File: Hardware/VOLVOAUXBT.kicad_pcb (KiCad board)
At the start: 2 copper layers, 100 x 35 mm, 66 parts, among them J1 10118193-0001LF, J10 Conn_01x02_Pin, J11 Conn_01x02_Pin, J12 Conn_01x05_Pin, J13 Conn_01x05_Pin, J14 Conn_01x05_Pin, J15 Conn_01x02_Pin, J16 Conn_01x02_Pin, J17 Conn_01x01_Pin, J18 Conn_01x02_Pin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

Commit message: Before swap to wroom
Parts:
- moved C2 122.7 mm to (161.3, 139.5), turned to -90 degrees
- moved C1 117.8 mm to (158.8, 139.5), turned to -90 degrees
- moved U1 109.0 mm to (156.2, 137.2), turned to 180 degrees
- moved C4 105.6 mm to (153.3, 141.0), turned to 0 degrees
- moved C3 104.1 mm to (153.3, 138.5), turned to 0 degrees
- moved J11 86.3 mm to (160.0, 144.8), turned to -90 degrees
- moved C10 79.2 mm to (147.3, 101.6), turned to 0 degrees
- moved C11 78.8 mm to (147.3, 99.1), turned to 0 degrees
- moved C20 77.6 mm to (141.8, 143.5), turned to 180 degrees
- moved C21 77.3 mm to (139.3, 145.6), turned to -90 degrees
- moved R10 76.9 mm to (146.1, 91.9), turned to -90 degrees
- moved C14 75.5 mm to (145.7, 96.5), turned to 0 degrees
- moved C17 74.3 mm to (143.5, 86.4), turned to 0 degrees
- moved R12 72.3 mm to (139.3, 142.2), turned to -90 degrees
- moved J18 71.9 mm to (138.0, 148.6), turned to -90 degrees
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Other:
- board size 100 x 35 mm -> 110 x 30 mm

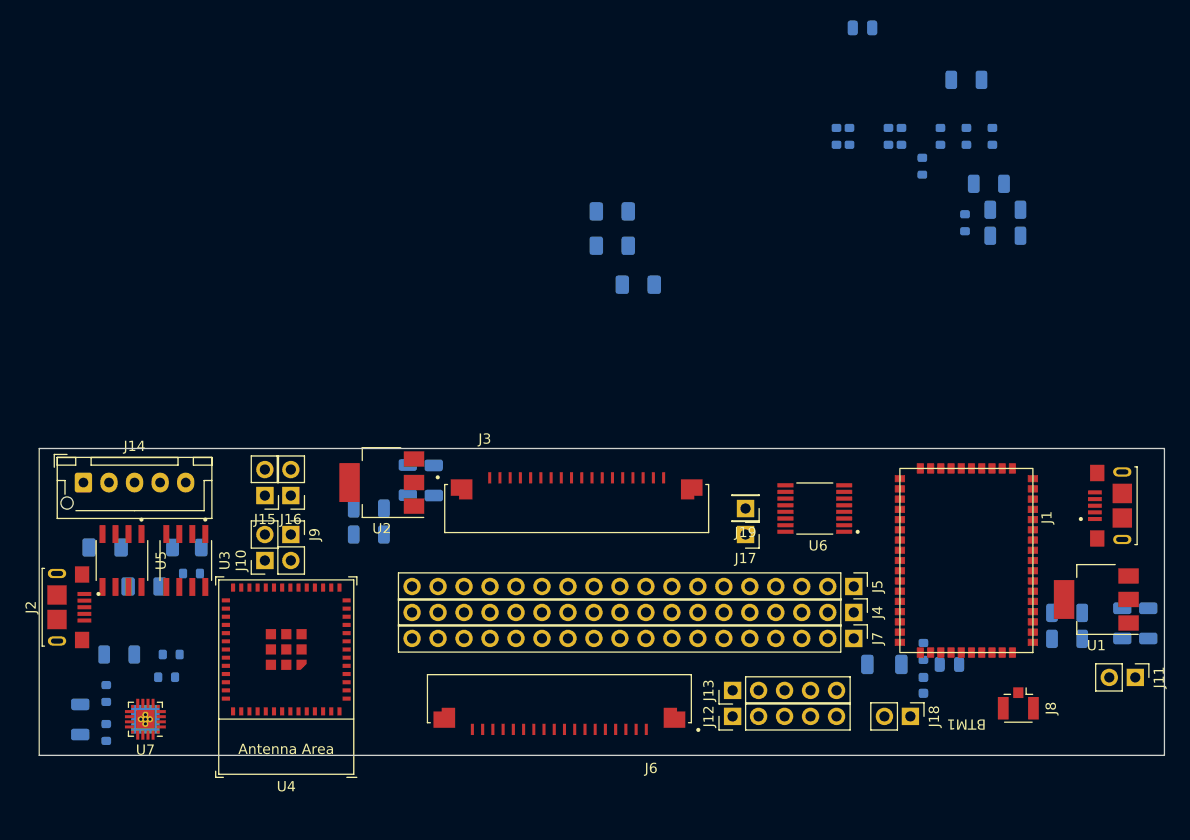
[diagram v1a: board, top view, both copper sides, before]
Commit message: Swap to ESP32-wroom-32e. Updated PCB too
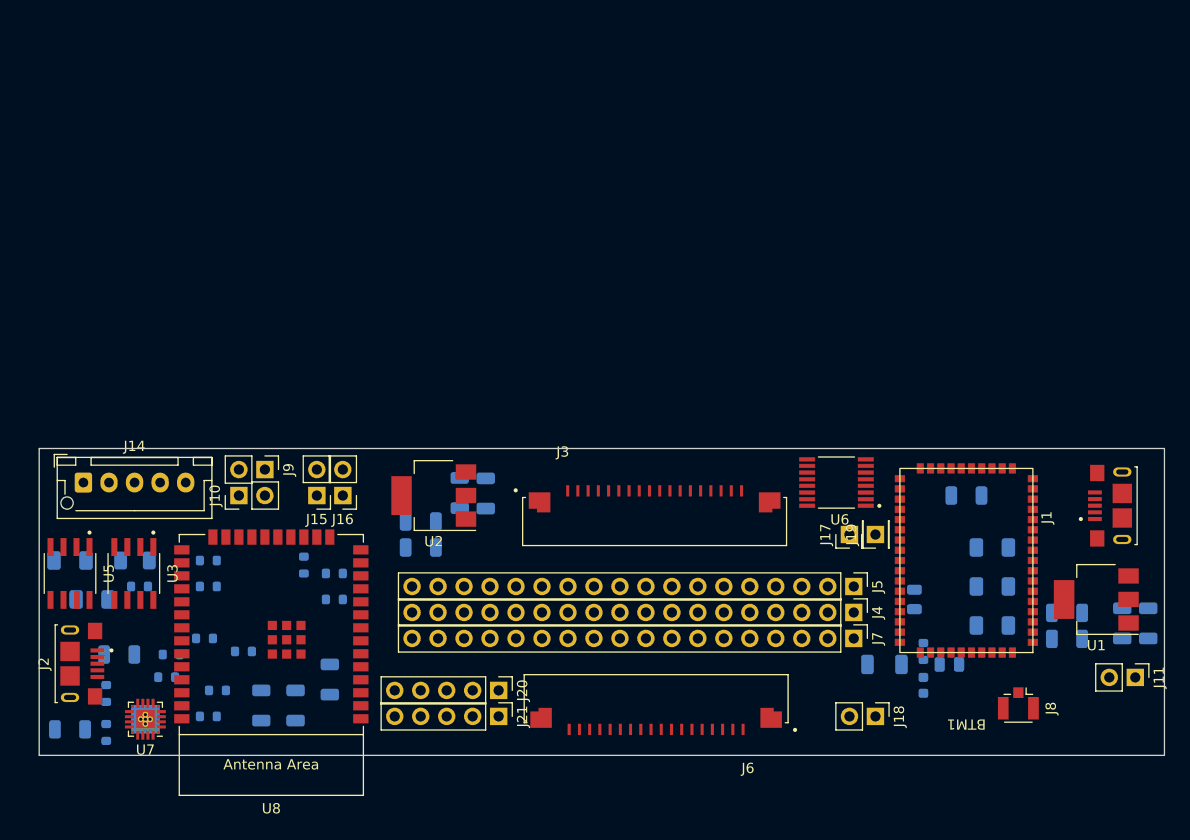
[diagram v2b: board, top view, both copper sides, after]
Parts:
- removed C10: 10uF/25V(20%), Capacitor_SMD:C_1206_3216Metric
- removed C11: 0.1uF/50V(10%), Capacitor_SMD:C_1206_3216Metric
- removed C14: 1uF/16V(10%), Capacitor_SMD:C_1206_3216Metric
- removed J12, J13: Conn_01x05_Pin, Connector_PinHeader_2.54mm:PinHeader_1x05_P2.54mm_Vertical
- removed R1: 10K(1%), Resistor_SMD:R_0603_1608Metric
- removed R10, R3, R4, R5, R6, R7, R8, R9: 500, Resistor_SMD:R_0603_1608Metric
- removed U4: ESP32-MINI-1, PCM_Espressif:ESP32-MINI-1
- added C23: 1uF/16V(10%), Capacitor_SMD:C_1206_3216Metric, B.Cu at (81.3, 145.0)
- added C24: 10uF/25V(20%), Capacitor_SMD:C_1206_3216Metric, B.Cu at (77.9, 147.5)
- added C25: 0.1uF/50V(10%), Capacitor_SMD:C_1206_3216Metric, B.Cu at (74.6, 147.5)
- added J20: Conn_01x05_Pin, Connector_PinHeader_2.54mm:PinHeader_1x05_P2.54mm_Vertical, F.Cu at (97.8, 146.1)
- added J21: Conn_01x05_Pin, Connector_PinHeader_2.54mm:PinHeader_1x05_P2.54mm_Vertical, F.Cu at (97.8, 148.6)
- added R16: 10K(1%), Resistor_SMD:R_0603_1608Metric, B.Cu at (72.8, 142.2)
- added R17: 500, Resistor_SMD:R_0603_1608Metric, B.Cu at (78.7, 133.8)
- added R18: 500, Resistor_SMD:R_0603_1608Metric, B.Cu at (81.7, 134.6)
- added R19: 500, Resistor_SMD:R_0603_1608Metric, B.Cu at (69.4, 148.6)
- added R20: 500, Resistor_SMD:R_0603_1608Metric, B.Cu at (81.7, 137.2)
- added R21: 500, Resistor_SMD:R_0603_1608Metric, B.Cu at (69.4, 133.3)
- added R22: 500, Resistor_SMD:R_0603_1608Metric, B.Cu at (69.4, 135.9)
- added R23: 500, Resistor_SMD:R_0603_1608Metric, B.Cu at (69.0, 141.0)
- added R24: 500, Resistor_SMD:R_0603_1608Metric, B.Cu at (70.3, 146.1)
- added U8: ESP32-WROOM-E, PCM_Espressif:ESP32-WROOM-32E, F.Cu at (75.6, 141.8)
- moved C15 56.1 mm to (138.4, 137.2), turned to 90 degrees
- moved C9 54.9 mm to (146.1, 139.7), turned to 0 degrees
- moved C12 49.9 mm to (146.1, 135.9), turned to 0 degrees
- moved C13 43.1 mm to (146.1, 132.1)
- moved C17 40.6 mm to (143.5, 127.0)
- moved J19 13.0 mm to (134.6, 130.8), turned to 90 degrees
- moved J17 10.2 mm to (132.1, 130.8), turned to 90 degrees
- moved J6 9.46 mm to (113.2, 146.9)
- moved J3 7.73 mm to (113.0, 129.5)
- moved J9 6.84 mm to (74.9, 124.5)
- moved J10 6.84 mm to (72.4, 127.0)
- moved J2 5.66 mm to (55.9, 143.4)
- moved U3 5.24 mm to (62.1, 134.6)
- moved C16 5.24 mm to (58.0, 137.2)
- moved C7 5.24 mm to (90.2, 132.1)
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
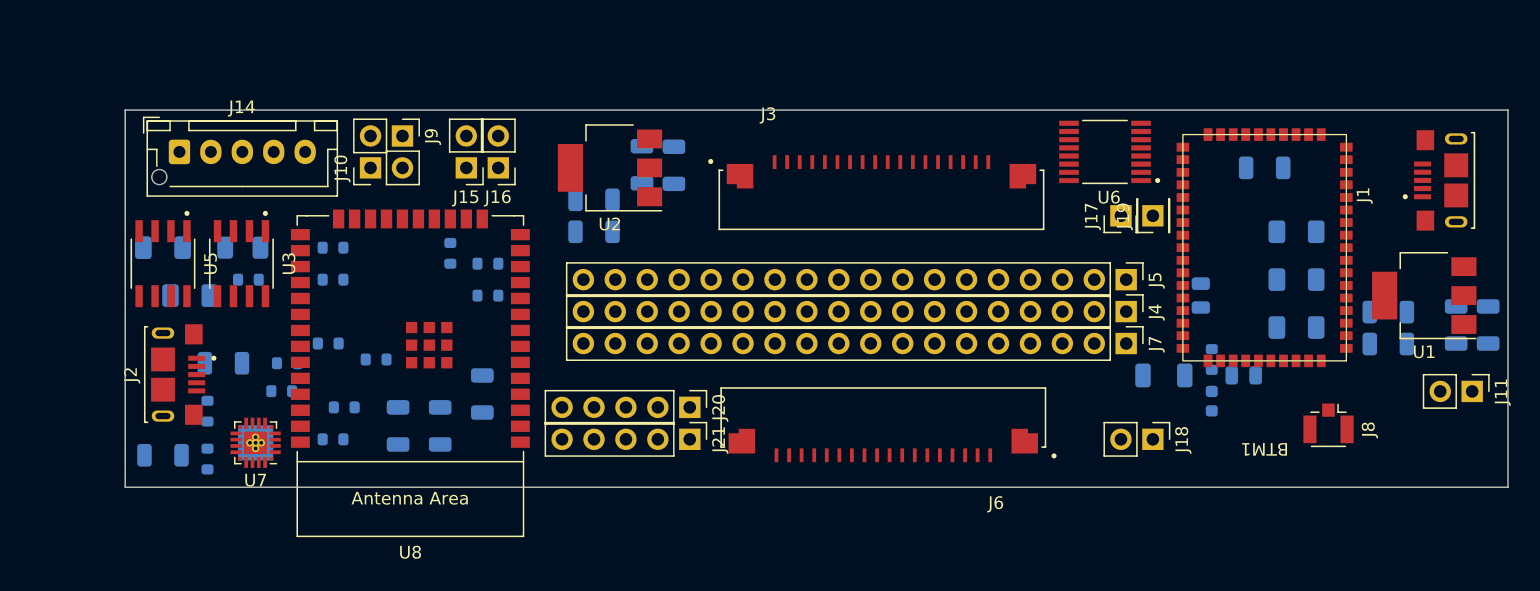
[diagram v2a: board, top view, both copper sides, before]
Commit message: First iteration of PCB routing
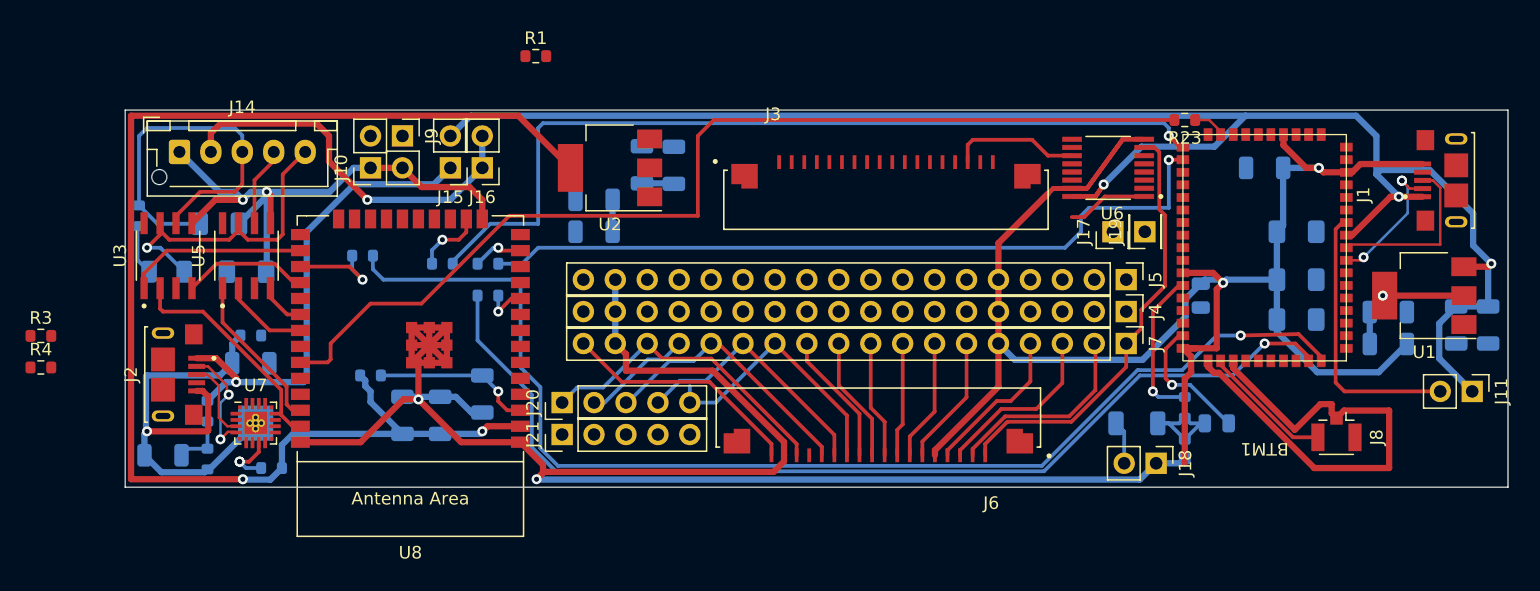
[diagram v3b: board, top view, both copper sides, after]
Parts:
- removed R19, R22, R24: 500, Resistor_SMD:R_0603_1608Metric
- added R1: 500, Resistor_SMD:R_0603_1608Metric, F.Cu at (85.5, 118.1)
- added R3: 500, Resistor_SMD:R_0603_1608Metric, F.Cu at (46.2, 140.4)
- added R4: 500, Resistor_SMD:R_0603_1608Metric, F.Cu at (46.2, 142.9)
- R23: moved to F.Cu
- moved R23 70.4 mm to (137.2, 123.2)
- moved J20 10.2 mm to (87.6, 145.7), turned to 90 degrees
- moved J21 10.2 mm to (87.6, 148.2), turned to 90 degrees
- moved R2 10.1 mm to (54.0, 130.8), turned to 90 degrees
- moved C18 6.91 mm to (62.5, 135.3), turned to 0 degrees
- moved U5 6.67 mm to (62.5, 134.0), turned to 90 degrees
- moved D1 6.35 mm to (56.2, 135.3), turned to 0 degrees
- moved R11 6.17 mm to (64.5, 150.9)
- moved C16 6.17 mm to (60.4, 131.4), turned to 0 degrees
- moved U3 5.87 mm to (56.3, 134.0), turned to 90 degrees
- moved C20 4.37 mm to (139.7, 147.3)
- moved C21 4.37 mm to (137.2, 149.4)
- moved L1 4.37 mm to (133.3, 147.3)
- moved R12 4.37 mm to (137.2, 146.1)
- moved R15 3.65 mm to (62.9, 140.3)
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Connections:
- J3 pad 14: /CD_GND -> GND
- J3 pad 2: /CD_GND -> GND
- J4 pad 17: /CD_GND -> GND
- J4 pad 5: /CD_GND -> GND
- J5 pad 1: /CD_I2S_LRCK -> unconnected-(J5-Pin_1-Pad1)
- J5 pad 17: /CD_GND -> GND
- J5 pad 5: /CD_GND -> GND
- J6 pad 17: /MB_GND -> GND
- J6 pad 5: /MB_GND -> GND
- J7 pad 17: /MB_GND -> GND
- J7 pad 5: /MB_GND -> GND
- U6 pad 16: VBUS -> BTM_USB_VBUS
- U8 pad 11: /LIN1_RXD -> Net-(U8-DAC_2/ADC2_CH9/GPIO26)
- U8 pad 12: /LIN1_TXD -> /MUX_CONT
- U8 pad 26: /MUX_CONT -> /LIN1_RXD
- U8 pad 28: Net-(U8-GPIO17) -> /LIN1_TXD
- U8 pad 31: /LIN2_RXD -> /LIN2_SLP
- U8 pad 36: Net-(U8-GPIO22) -> /LIN2_RXD
- U8 pad 37: Net-(U8-GPIO23) -> /LIN1_SLP
- U8 pad 8: /LIN2_SLP -> Net-(U8-32K_XP/GPIO32/ADC1_CH4)
- U8 pad 9: /LIN1_SLP -> Net-(U8-32K_XN/GPIO33/ADC1_CH5)
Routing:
- net GND: track 0.00 -> 407.7 mm, vias 0 -> 7
- net BTM_USB_VBUS: track 0.00 -> 135.0 mm, vias 0 -> 3
- net VCC_3V3: track 0.00 -> 105.5 mm, vias 0 -> 2
- net /BTM_PREVIOUS: track 0.00 -> 95.5 mm, vias 0 -> 1
- net Net-(U8-GPIO21): track 0.00 -> 82.2 mm
- net /BTM_NEXT: track 0.00 -> 81.7 mm, vias 0 -> 1
- net /BTM_GPIO_R2: track 0.00 -> 68.5 mm, vias 0 -> 1
- net /BTM_GPIO_R1: track 0.00 -> 60.9 mm, vias 0 -> 1
- net VBUS: track 0.00 -> 38.8 mm, vias 0 -> 1
- net /MB_I2S_LRCK: track 0.00 -> 34.6 mm
- net /EXT_5V: track 0.00 -> 30.7 mm, vias 0 -> 1
- net /LIN1: track 0.00 -> 30.5 mm
- net Net-(D1-A): track 0.00 -> 26.0 mm, vias 0 -> 1
- net /MB_STM: track 0.00 -> 24.8 mm
- net Net-(BTM1-VCHG_SENSE): track 0.00 -> 21.9 mm
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
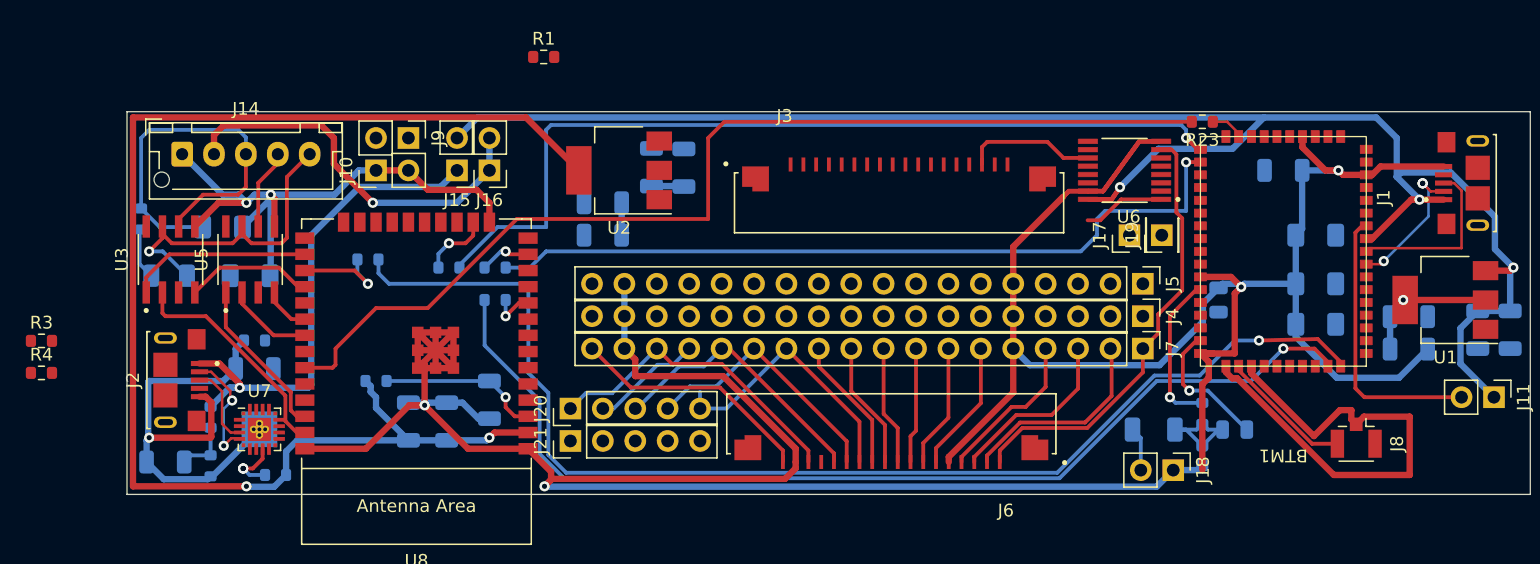
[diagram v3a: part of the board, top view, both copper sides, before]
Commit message: Crappy routing, too cramped
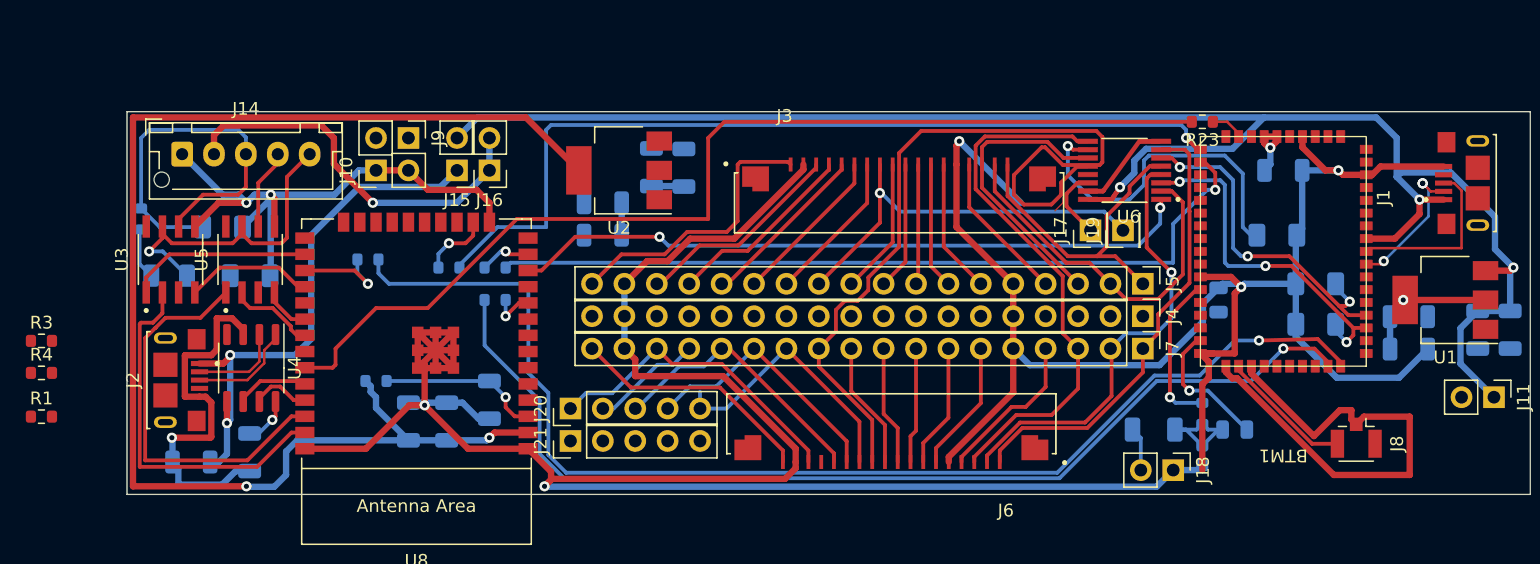
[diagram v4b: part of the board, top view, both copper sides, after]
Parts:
- removed C19: 10uF/25V(20%), Capacitor_SMD:C_1206_3216Metric
- removed C22: 1uF/16V, Capacitor_SMD:C_1206_3216Metric
- removed R11: 1K, Resistor_SMD:R_0603_1608Metric
- removed R13: 22.1K, Resistor_SMD:R_0603_1608Metric
- removed R14: 47.5K, Resistor_SMD:R_0603_1608Metric
- removed R15: 10k(NC), Resistor_SMD:R_0603_1608Metric
- removed U7: CP2102N-Axx-xQFN20, Package_DFN_QFN:SiliconLabs_QFN-20-1EP_3x3mm_P0.5mm_EP1.8x1.8mm_ThermalVias
- added C10: 0.1uF/25V(20%), Capacitor_SMD:C_1206_3216Metric, B.Cu at (57.9, 149.9)
- added C11: 0.1uF/25V(20%), Capacitor_SMD:C_1206_3216Metric, B.Cu at (62.5, 149.1)
- added U4: CH340N, Package_SO:SOP-8_3.9x4.9mm_P1.27mm, F.Cu at (62.6, 142.5)
- moved R1 48.4 mm to (46.2, 146.3)
- moved J17 3.07 mm to (128.4, 131.7)
- moved J19 3.07 mm to (130.9, 131.7)
- moved C13 3.05 mm to (143.0, 132.1), turned to 180 degrees
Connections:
- J5 pad 1: unconnected-(J5-Pin_1-Pad1) -> /CD_I2S_LRCK
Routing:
- net /MB_ACC-ON: track 10.6 -> 65.9 mm
- net /MUX_CONT: track 6.44 -> 53.6 mm, vias 0 -> 2
- net /CD_ACC-ON: track 0.00 -> 31.6 mm, vias 0 -> 1
- net /CD_I2S_DATA: track 0.00 -> 28.9 mm
- net /MB_I2S_BCK: track 13.9 -> 42.4 mm
- net /BT_I2S_DATA: track 0.00 -> 27.9 mm, vias 0 -> 3
- net /BT_I2S_BCK: track 0.00 -> 27.4 mm, vias 0 -> 1
- net /BT_I2S_LRCK: track 0.00 -> 27.3 mm, vias 0 -> 3
- net /CD_I2S_LRCK: track 0.00 -> 25.6 mm
- net /CD-8V: track 0.00 -> 22.2 mm
- net GND: track 407.7 -> 429.6 mm, vias 7 -> 8
- net Net-(BTM1-VCHG_SENSE): track 21.9 -> 0.32 mm
- net /MB_I2S_DATA: track 16.0 -> 34.7 mm, vias 0 -> 1
- net /LIN2_RXD: track 12.6 -> 31.3 mm
- net /CD_STM: track 0.00 -> 16.5 mm
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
